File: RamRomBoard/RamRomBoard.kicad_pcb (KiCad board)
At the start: 2 copper layers, 100 x 100 mm, 97 parts, among them J1 BUS, J10 Micro_SD_Card_Det2, J2 BUS, J3 Spare, J4 Spare, J5 Screw_Terminal_01x02, J6 USB_B_Micro, J7 STM32F401, J8 Dual LED Socket, J9 JTAG, SW1 033TBVSA, SW2 SW_Push, U1 74LVC125, U10 74AHC1G14, U11 IS61WV102416FBLL1T2, U12 IS61WV10248EDBLL-10TL, U13 74LVC595, U14 74LVC595, U15 SN74LVC245ANSR, U16 SN74LVC245ANSR, U17 74LVC595, U18 74HC165, U19 SN74LVC245ANSR, U2 AZ1117-3.3, U20 DS1314, U3 74LVC08AD, U4 DS1085, U5 74LVC1G32, U6 74AHC1G14, U7 74HC590, U8 74HC590, U9 74HC590

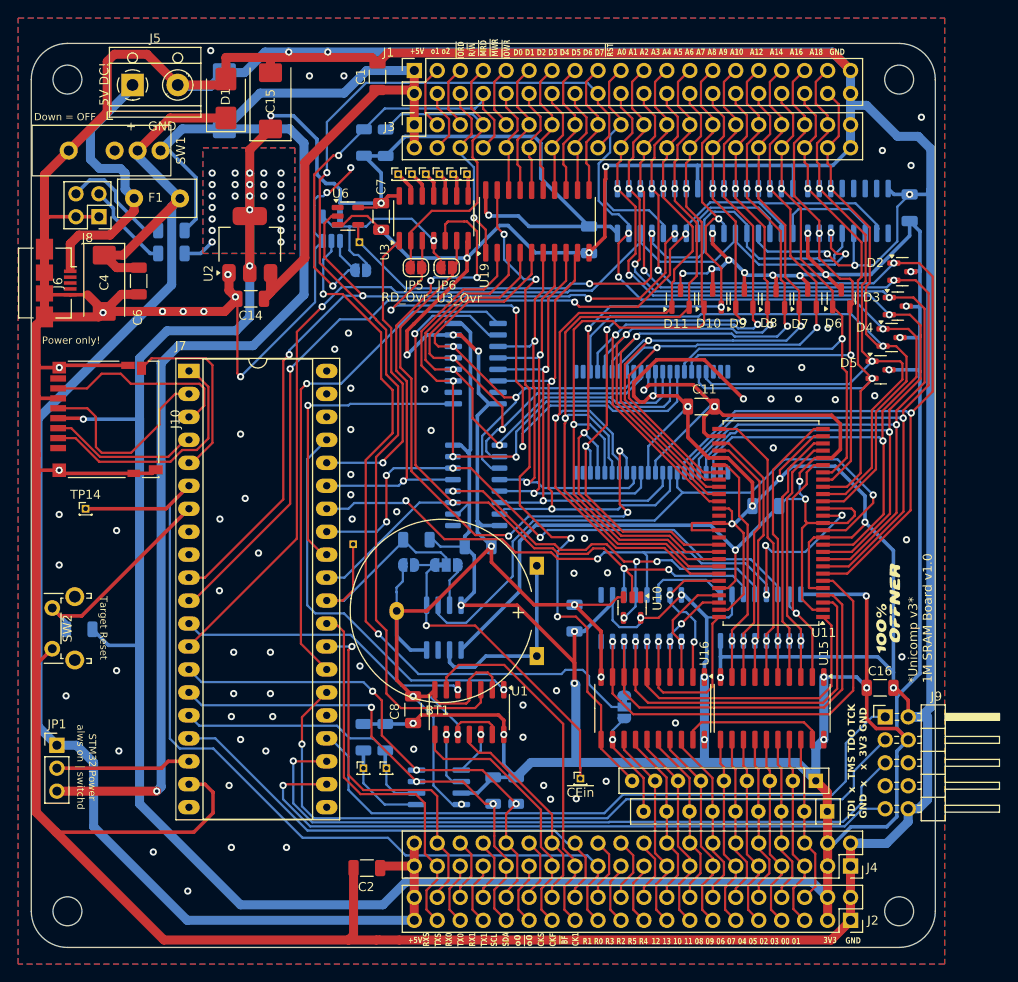
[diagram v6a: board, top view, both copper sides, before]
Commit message: first boards manufactured
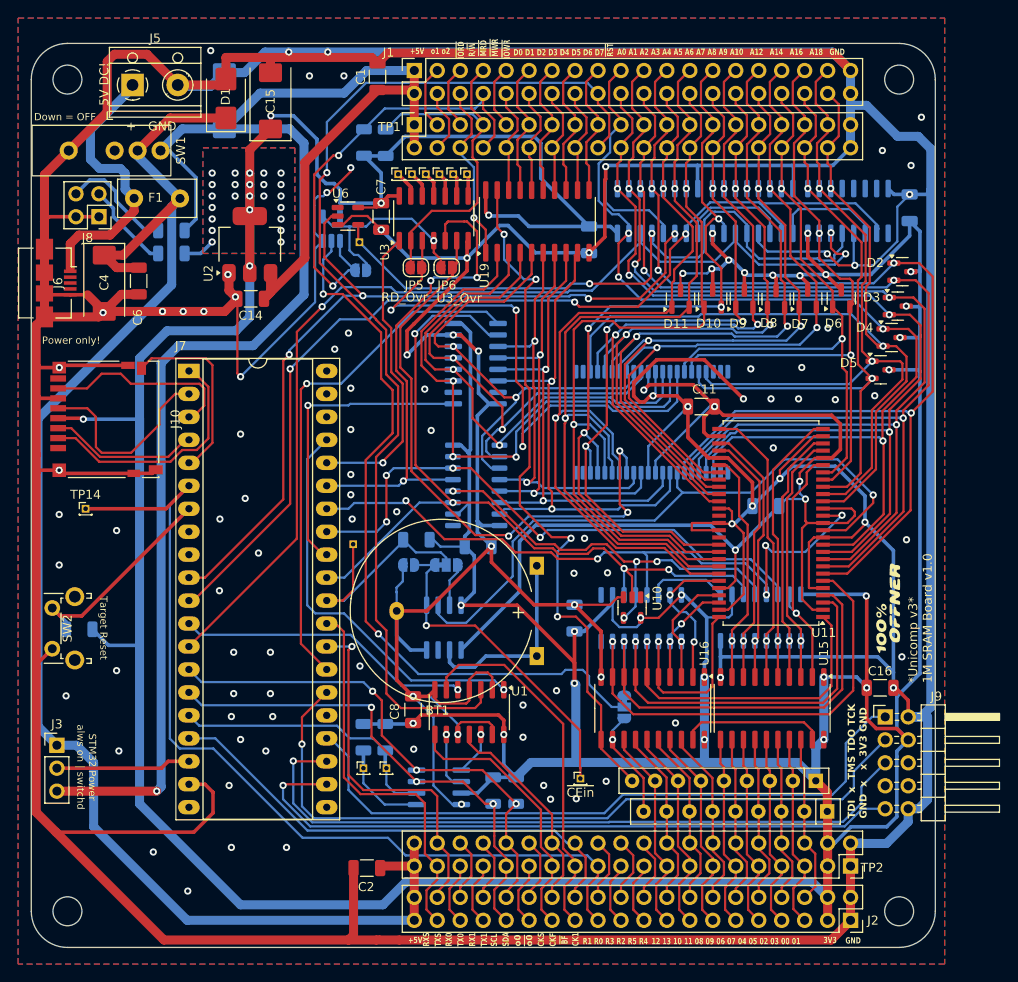
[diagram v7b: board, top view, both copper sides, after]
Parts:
- R1: value 560E -> 1k
- R3, R4: value 3k3 -> 1k
- R5, R6: value 3k3 -> 10k
- R7, R8: value 10k -> 1k
- renumbered JP1 to J3, J3 to TP1, TP1 to TP12, TP2 to TP13, J4 to TP2
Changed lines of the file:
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@@
 	(net 119 "unconnected-(J9-Pin_6-Pad6)")
 	(net 120 "unconnected-(J9-Pin_8-Pad8)")
-	(net 121 "Net-(TP2-Pad1)")
+	(net 121 "Net-(TP12-Pad1)")
 	(net 122 "Net-(TP3-Pad1)")
 	(net 123 "Net-(TP4-Pad1)")
@@
 	(net 133 "Net-(J8-Pin_3)")
 	(net 134 "Net-(J8-Pin_4)")
-	(net 135 "Net-(TP1-Pad1)")
+	(net 135 "Net-(TP13-Pad1)")
 	(net 136 "Net-(JP5-A)")
 	(net 137 "Net-(JP6-A)")
@@
 	(net 179 "/~{BW}")
 	(net 180 "/~{EXTRST}")
-	(net 181 "Net-(J7-Pin_18)")
+	(net 181 "Net-(J3-C)")
 	(net 182 "/~{CS_SD}")
 	(net 183 "/MOSI_SD")
@@
 			(layers "*.Cu" "*.Mask")
 			(remove_unused_layers no)
-			(net 181 "Net-(J7-Pin_18)")
+			(net 181 "Net-(J3-C)")
 			(pinfunction "Pin_18")
 			(pintype "passive")
@@
 		(descr "Through hole straight pin header, 1x01, 1.00mm pitch, single row")
 		(tags "Through hole pin header THT 1x01 1.00mm single row")
-		(property "Reference" "TP1"
+		(property "Reference" "TP12"
 			(at 0 -1.56 0)
 			(layer "F.SilkS")
@@
 			(layers "*.Cu" "*.Mask")
 			(remove_unused_layers no)
-			(net 135 "Net-(TP1-Pad1)")
+			(net 121 "Net-(TP12-Pad1)")
 			(pinfunction "1")
 			(pintype "passive")
@@
 		(descr "Through hole straight socket strip, 2x20, 2.54mm pitch, double cols (from Kicad 4.0.7), script generated")
 		(tags "Through hole socket strip THT 2x20 2.54mm double row")
-		(property "Reference" "J4"
+		(property "Reference" "TP2"
 			(at 0.1732 -2.375 180)
 			(layer "F.SilkS")
@@
 		(descr "Through hole straight pin header, 1x03, 2.54mm pitch, single row")
 		(tags "Through hole pin header THT 1x03 2.54mm single row")
-		(property "Reference" "JP1"
+		(property "Reference" "J3"
 			(at 0 -2.33 0)
 			(layer "F.SilkS")
@@
 		(sheetname "Root")
 		(sheetfile "RamRomBoard.kicad_sch")
-		(attr through_hole exclude_from_bom)
+		(attr through_hole)
 		(fp_line
 			(start -1.33 -1.33)
@@
 			(layers "*.Cu" "*.Mask")
 			(remove_unused_layers no)
-			(net 181 "Net-(J7-Pin_18)")
+			(net 181 "Net-(J3-C)")
 			(pinfunction "C")
 			(pintype "passive")
@@
 			(layers "F.Cu" "F.Paste" "F.Mask")
 			(roundrect_rratio 0.25)
-			(net 121 "Net-(TP2-Pad1)")
+			(net 135 "Net-(TP13-Pad1)")
 			(pintype "input")
 		)
@@
 			(layers "F.Cu" "F.Paste" "F.Mask")
 			(roundrect_rratio 0.25)
-			(net 135 "Net-(TP1-Pad1)")
+			(net 121 "Net-(TP12-Pad1)")
 			(pintype "input")
 		)
@@
 		(descr "Through hole straight pin header, 1x01, 1.00mm pitch, single row")
 		(tags "Through hole pin header THT 1x01 1.00mm single row")
-		(property "Reference" "TP2"
+		(property "Reference" "TP13"
 			(at 0 -1.56 0)
 			(layer "F.SilkS")
@@
 			(layers "*.Cu" "*.Mask")
 			(remove_unused_layers no)
-			(net 121 "Net-(TP2-Pad1)")
+			(net 135 "Net-(TP13-Pad1)")
 			(pinfunction "1")
 			(pintype "passive")
@@
 		(descr "Through hole straight socket strip, 2x20, 2.54mm pitch, double cols (from Kicad 4.0.7), script generated")
 		(tags "Through hole socket strip THT 2x20 2.54mm double row")
-		(property "Reference" "J3"
+		(property "Reference" "TP1"
 			(at -0.2328 -2.7558 180)
 			(layer "F.SilkS")
@@
 			)
 		)
-		(property "Value" "3k3"
+		(property "Value" "1k"
 			(at 0 -1.82 90)
 			(layer "B.Fab")
@@
 			)
 		)
-		(property "Value" "560E"
+		(property "Value" "1k"
 			(at 0 -1.82 180)
 			(layer "B.Fab")
@@
 			)
 		)
-		(property "Value" "10k"
+		(property "Value" "1k"
 			(at 0 -1.82 90)
 			(layer "B.Fab")
@@
 			)
 		)
-		(property "Value" "3k3"
+		(property "Value" "10k"
 			(at 0 -1.82 90)
 			(layer "F.Fab")
@@
 			)
 		)
-		(property "Value" "3k3"
+		(property "Value" "1k"
 			(at 0 -1.82 90)
 			(layer "B.Fab")
@@
 			)
 		)
-		(property "Value" "3k3"
+		(property "Value" "10k"
 			(at 0 -1.82 90)
 			(layer "B.Fab")
@@
 			)
 		)
-		(property "Value" "10k"
+		(property "Value" "1k"
 			(at 0 -1.82 90)
 			(layer "B.Fab")
@@
 	)
 	(segment
-		(start 97.059 66.872795)
-		(end 97.059 64.853995)
+		(start 95.789 66.872795)
+		(end 95.789 65.105995)
 		(width 0.4)
 		(layer "F.Cu")
@@
 	)
 	(segment
-		(start 97.059 64.853995)
-		(end 96.676 64.470995)
+		(start 95.789 65.105995)
+		(end 95.154 64.470995)
 		(width 0.4)
 		(layer "F.Cu")
@@
 	)
 	(segment
-		(start 95.789 66.872795)
-		(end 95.789 65.105995)
+		(start 97.059 66.872795)
+		(end 97.059 64.853995)
 		(width 0.4)
 		(layer "F.Cu")
@@
 	)
 	(segment
-		(start 95.789 65.105995)
-		(end 95.154 64.470995)
+		(start 97.059 64.853995)
+		(end 96.676 64.470995)
 		(width 0.4)
 		(layer "F.Cu")
